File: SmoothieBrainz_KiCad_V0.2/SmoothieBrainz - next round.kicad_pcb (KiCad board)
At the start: 2 copper layers, 100 x 80 mm, 127 parts, among them IC1 LPC1769, IC5 LD117ADT33TR, Q1 BSL207SP, Q2 12MHz, SW1 SW_TACT_4P_B, SW3 SW_TACT_4P_B, U2 HC_05, U3 USD-SOCKETUSD, X14 USB

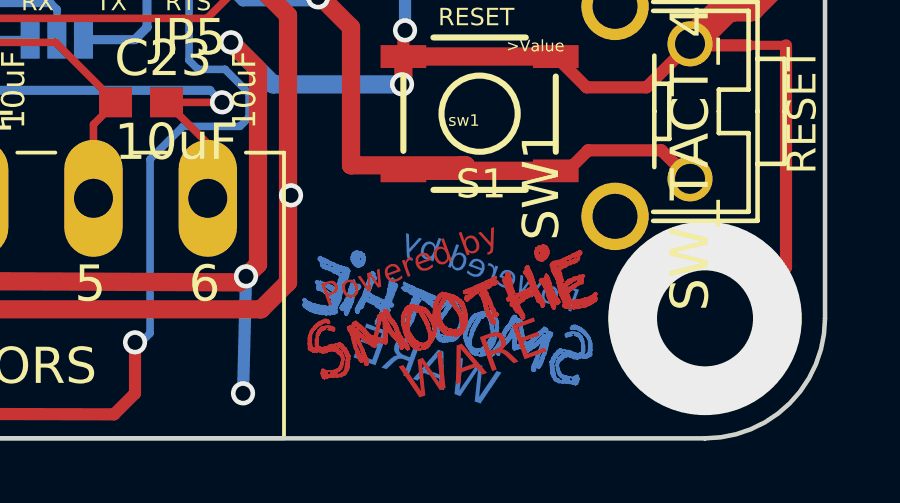
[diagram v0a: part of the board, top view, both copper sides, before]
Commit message: Cleaned up logo
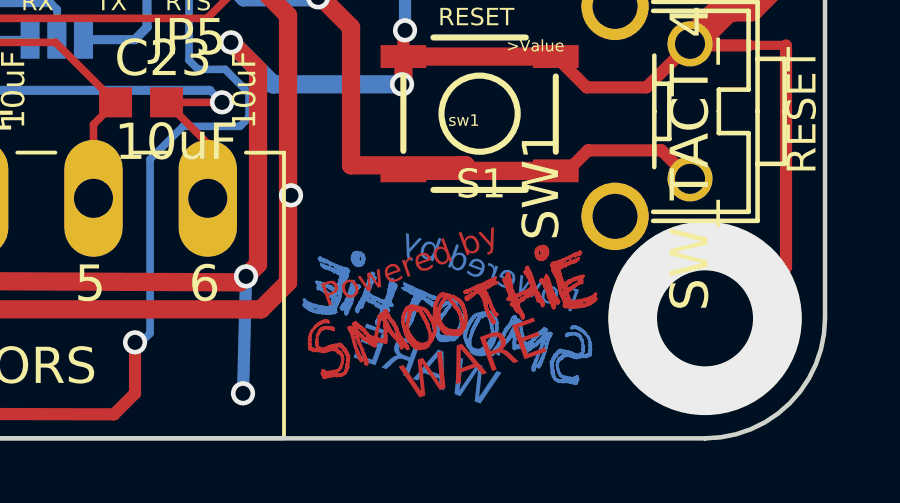
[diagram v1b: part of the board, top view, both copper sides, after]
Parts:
- added ?: , LOGO, B.Cu at (191.7, 138.6)
- added ?: , LOGO, F.Cu at (180.3, 138.4)
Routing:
- removed copper zone on B.Cu, net (none)
- removed copper zone on F.Cu, net (none)
